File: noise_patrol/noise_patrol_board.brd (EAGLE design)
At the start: 53.3 x 57.1 mm, 13 parts, among them IC1 4511D, Q1 TIP31C, U1 OPA345NA/3K

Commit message: Saving Progress: Added More parts and starting to understand the software
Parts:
- added C1: 2.2\muF, SparkFun-Capacitors:0603
- added MK1: MIC-PTH, SparkFun-Sensors:MICROPHONE-PTH-9.7MM
- added R8: (no value), rcl:M1206
- R1, R2, R3, R4, R5, R6, R7: value (none) -> 220
- moved R7 152.3 mm to (41.9, 20.3)
- moved R6 151.7 mm to (41.9, 24.1)
- moved R5 151.1 mm to (41.9, 27.9)
- moved R4 150.5 mm to (41.9, 31.8)
- moved R3 149.9 mm to (41.9, 35.6)
- moved R2 149.4 mm to (41.9, 39.4)
- moved R1 148.8 mm to (41.9, 43.2)
- moved LED1 147.7 mm to (64.8, 29.2)
- moved D1 123.7 mm to (14.0, 50.8)
- moved Q1 114.5 mm to (2.54, 63.5)
- moved U1 106.7 mm to (35.6, 8.89)
- moved IC1 94.6 mm to (21.6, 30.5), turned to 270 degrees
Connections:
- net N$1 renamed TOOL
- net V+ renamed +5V
- removed net V-: U1.2
- new net 5V: IC1.3, IC1.4, R8.1
- new net GND: LED1.1, LED1.6, U1.2
- new net N$14: B1.D4, IC1.7
- new net N$15: B1.D5, IC1.1
- new net N$16: B1.D6, IC1.2
- new net N$17: B1.D7, IC1.6
- new net N$18: B1.A0, U1.1
- new net N$19: B1.D8, IC1.5
- new net N$20: C1.1, MK1.OUT, R8.2

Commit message: Starting to Rearrange the board
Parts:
- added C2: 2.2\muF, SparkFun-Capacitors:0603
- added C3: 15pF, SparkFun-Capacitors:0603
- added R10, R11, R12: 100k, rcl:M1206
- added R9: 75k, rcl:M1206
- added X1: (no value), con-wago-508:W237-9P
- R8: value (none) -> 13.7k
- moved C1 138.8 mm to (33.0, 54.6)
- moved MK1 123.3 mm to (33.0, 44.5), turned to 90 degrees
- moved R8 94.3 mm to (8.89, 6.35)
- moved B1 86.4 mm to (45.7, 44.5)
- moved Q1 60.2 mm to (55.9, 35.6)
- moved D1 53.1 mm to (63.5, 31.8), turned to 90 degrees
- moved R4 34.2 mm to (50.8, 64.8)
- moved LED1 33.2 mm to (61.0, 62.2), turned to 180 degrees
- moved IC1 31.8 mm to (40.6, 55.9)
- moved U1 29.3 mm to (7.62, 17.8)
- moved R5 28.1 mm to (50.8, 54.6)
- moved R3 28.1 mm to (50.8, 62.2)
- moved R2 22.2 mm to (50.8, 59.7)
- moved R1 16.6 mm to (50.8, 57.1)
- moved R7 10.9 mm to (35.6, 29.2)
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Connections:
- removed net +5V: U1.5
- new net N$21: C1.2, C2.1, R9.1, U1.4
- new net N$22: B1.D3, R12.1
- new net N$23: Q1.1, R12.2
- new net N$24: C3.1, R10.2, R11.1, U1.3
- new net N$25: D1.A, Q1.2, X1.1
- new net N$26: D1.C, X1.2
- net 5V: now also R10.1, U1.5
- net GND: now also C3.2, MK1.GND, Q1.3, R11.2
- net N$18: now also C2.2, R9.2
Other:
- board size 53.3 x 57.1 mm -> 100 x 80 mm

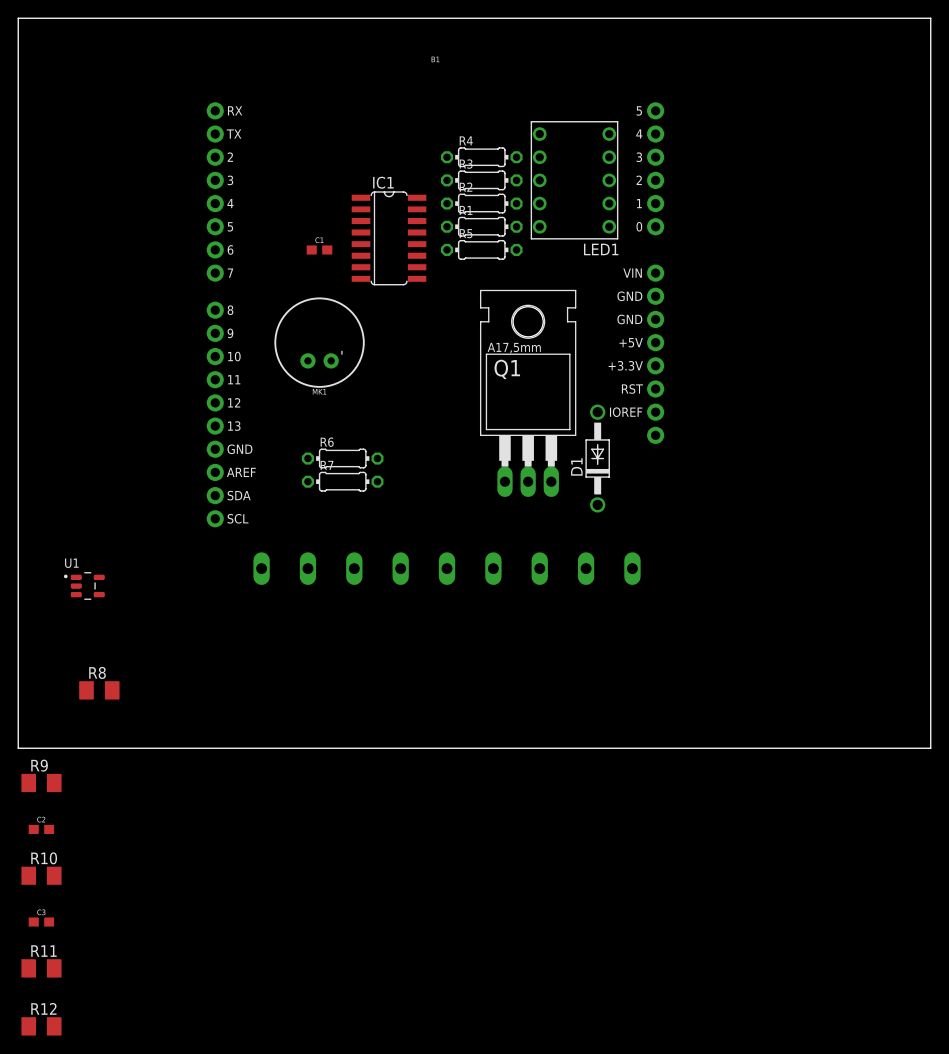
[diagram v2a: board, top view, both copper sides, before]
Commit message: Finished getting everything on to the board
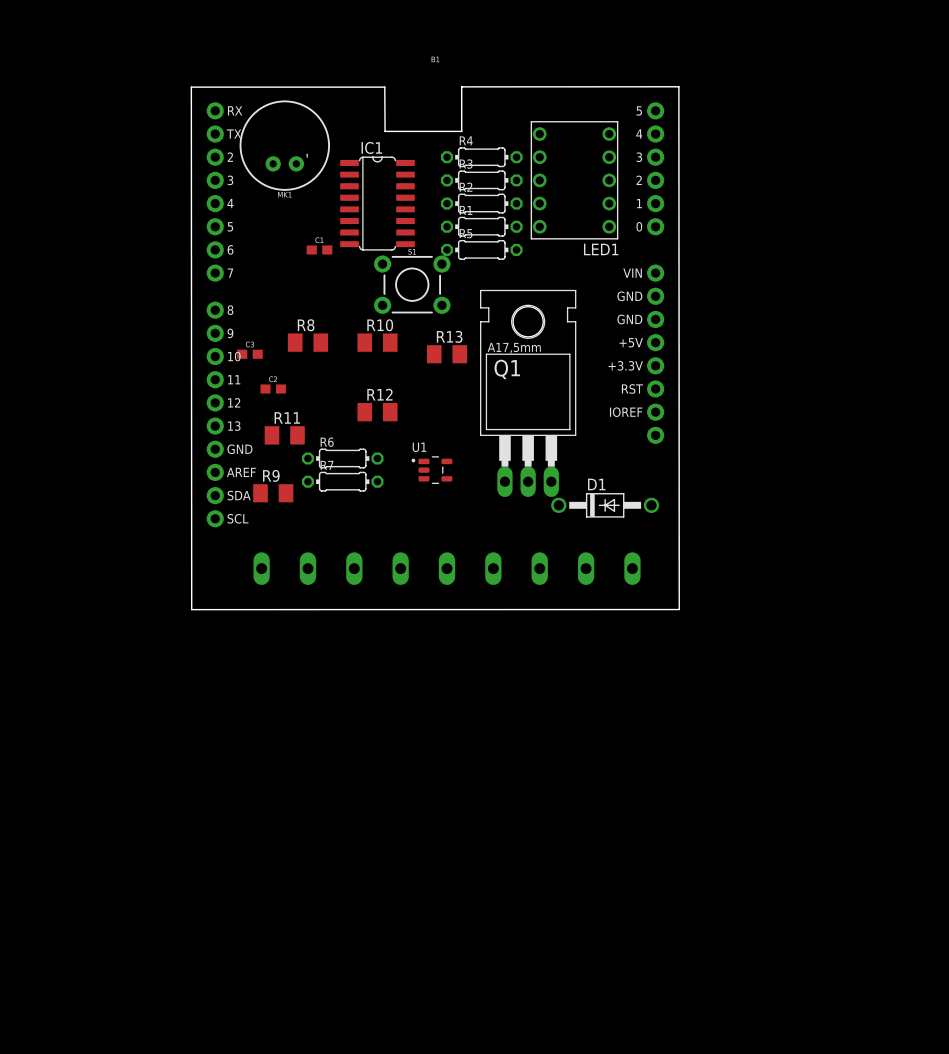
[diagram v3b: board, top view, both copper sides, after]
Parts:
- added R13: 10k, rcl:M1206
- added S1: MOMENTARY-SWITCH-SPST-PTH-6.0MM, SparkFun-Switches:TACTILE_SWITCH_PTH_6.0MM
- moved R12 76.7 mm to (39.4, 36.8)
- moved R10 69.1 mm to (39.4, 44.5)
- moved C3 66.3 mm to (25.4, 43.2)
- moved R11 64.2 mm to (29.2, 34.3)
- moved C2 54.5 mm to (27.9, 39.4)
- moved R8 44.4 mm to (31.8, 44.5)
- moved R9 40.7 mm to (27.9, 27.9)
- moved U1 40.2 mm to (45.7, 30.5)
- moved MK1 21.9 mm to (29.2, 66.0)
- moved D1 5.20 mm to (64.3, 26.6), turned to 0 degrees
- moved IC1 4.02 mm to (39.4, 59.7)
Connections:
- new net N$27: B1.D2, R13.2, S1.3
- net 5V: now also S1.1
- net GND: now also R13.1
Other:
- board size 100 x 80 mm -> 53.5 x 57.3 mm

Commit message: Finished
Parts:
- S1: value MOMENTARY-SWITCH-SPST-PTH-6.0MM -> Reset button
- moved R9 47.0 mm to (63.5, 58.7), turned to 270 degrees
- moved C2 42.9 mm to (66.5, 58.1), turned to 270 degrees
- moved R11 37.7 mm to (57.5, 59.1), turned to 270 degrees
- moved D1 32.7 mm to (31.6, 28.0), turned to 180 degrees
- moved C3 32.3 mm to (53.2, 59.7), turned to 270 degrees
- moved C1 31.8 mm to (63.7, 63.1), turned to 270 degrees
- moved R13 29.7 mm to (27.3, 65.3), turned to 180 degrees
- moved MK1 29.4 mm to (58.6, 67.5)
- moved U1 29.3 mm to (43.7, 59.8), turned to 180 degrees
- moved R12 26.8 mm to (27.2, 60.7)
- moved R7 26.5 mm to (43.3, 54.6)
- moved R6 26.2 mm to (43.3, 56.8)
- moved Q1 22.2 mm to (33.7, 36.2), turned to 270 degrees
- moved R10 21.3 mm to (43.5, 65.4)
- moved R4 20.7 mm to (43.1, 45.5)
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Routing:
- net GND: track 0.00 -> 121.9 mm, vias 0 -> 2
- net 5V: track 0.00 -> 53.8 mm, vias 0 -> 5
- net N$21: track 0.00 -> 32.8 mm, vias 0 -> 2
- net N$20: track 0.00 -> 30.3 mm, vias 0 -> 2
- net N$18: track 0.00 -> 29.7 mm, vias 0 -> 2
- net N$24: track 0.00 -> 27.7 mm
- net N$23: track 0.00 -> 27.5 mm, vias 0 -> 1
- net N$13: track 0.00 -> 24.1 mm
- net N$25: track 0.00 -> 20.1 mm
- net N$12: track 0.00 -> 20.0 mm
- net N$9: track 0.00 -> 18.2 mm, vias 0 -> 2
- net N$14: track 0.00 -> 17.6 mm, vias 0 -> 2
- net N$8: track 0.00 -> 16.8 mm
- net N$11: track 0.00 -> 15.9 mm
- net N$27: track 0.00 -> 15.4 mm
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- added copper zone on layer 16, net GND
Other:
- outline, holes or cut-outs redrawn

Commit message: Final
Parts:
- R12: value 100k -> 1k
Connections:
- removed net N$26: D1.C, X1.2
- net 5V: now also D1.C, X1.2
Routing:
- net 5V: track 53.8 -> 96.1 mm, vias 5 -> 7
- net N$26: track 8.93 -> 0.00 mm
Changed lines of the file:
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@@
 <attribute name="VALUE" x="56.93" y="60.83" size="1.27" layer="27" rot="R270"/>
 </element>
-<element name="R12" library="rcl" library_urn="urn:adsk.eagle:library:334" package="M1206" package3d_urn="urn:adsk.eagle:package:23566/2" value="100k" x="27.18" y="60.67" smashed="yes">
+<element name="R12" library="rcl" library_urn="urn:adsk.eagle:library:334" package="M1206" package3d_urn="urn:adsk.eagle:package:23566/2" value="1k" x="27.18" y="60.67" smashed="yes">
 <attribute name="NAME" x="26.14" y="61.98" size="1.27" layer="25"/>
 <attribute name="POPULARITY" value="22" x="27.18" y="60.67" size="1.778" layer="27" display="off"/>
@@
 <wire x1="34.7012" y1="59.86145625" x2="34.7012" y2="61.60454375" width="0.6" layer="1"/>
 <wire x1="33.34974375" y1="57.96" x2="33.71" y2="57.96" width="0.6" layer="1"/>
+<contactref element="D1" pad="C"/>
+<contactref element="X1" pad="2"/>
+<wire x1="36.73" y1="27.96" x2="36.73" y2="25.835" width="1.2" layer="1"/>
+<wire x1="36.73" y1="25.835" x2="31.92" y2="21.025" width="1.2" layer="1"/>
+<via x="33.52" y="45.81" extent="1-16" drill="0.8"/>
+<wire x1="36.73" y1="27.96" x2="36.73" y2="42.6" width="0.6" layer="16"/>
+<wire x1="36.73" y1="42.6" x2="33.52" y2="45.81" width="0.6" layer="16"/>
+<via x="27.13" y="45.6" extent="1-16" drill="0.8"/>
+<wire x1="33.52" y1="45.81" x2="33.31" y2="45.6" width="0.6" layer="1"/>
+<wire x1="33.31" y1="45.6" x2="27.13" y2="45.6" width="0.6" layer="1"/>
+<wire x1="27.13" y1="45.6" x2="27.13" y2="47.88425625" width="0.6" layer="16"/>
+<wire x1="27.13" y1="47.88425625" x2="27.1512" y2="47.90545625" width="0.6" layer="16"/>
+<wire x1="27.1512" y1="47.90545625" x2="27.1512" y2="53.0488" width="0.6" layer="16"/>
+<wire x1="27.1512" y1="53.0488" x2="26.96" y2="53.24" width="0.6" layer="16"/>
 </signal>
 <signal name="N$18">
@@
 <wire x1="23.8878" y1="36.25" x2="27.37" y2="36.25" width="1.2" layer="1"/>
 </signal>
-<signal name="N$26">
-<contactref element="D1" pad="C"/>
-<contactref element="X1" pad="2"/>
-<wire x1="31.92" y1="21.025" x2="31.92" y2="23.15" width="1.2" layer="1"/>
-<wire x1="31.92" y1="23.15" x2="36.73" y2="27.96" width="1.2" layer="1"/>
-</signal>
 <signal name="N$27">
